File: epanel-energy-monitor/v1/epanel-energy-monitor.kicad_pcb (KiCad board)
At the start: 2 copper layers, 103 x 86.5 mm, 179 parts, among them J1 Conn_02x04_Odd_Even, J10 Screw_Terminal_01x02, J11 Screw_Terminal_01x02, J12 Screw_Terminal_01x02, J13 Screw_Terminal_01x02, J14 Screw_Terminal_01x02, J15 Screw_Terminal_01x02, J16 Screw_Terminal_01x02, J17 Screw_Terminal_01x02, J18 Screw_Terminal_01x02, J19 Screw_Terminal_01x02, J2 Screw_Terminal_01x02, J3 Conn_01x02_Male, J4 Screw_Terminal_01x02, J5 Screw_Terminal_01x02, J6 Screw_Terminal_01x02, J7 Screw_Terminal_01x02, J8 Screw_Terminal_01x02, J9 Screw_Terminal_01x02, Q1 BSS138, T1 230V - 6V, U1 LTV-814, U2 MCP3208, U3 MCP3208, U4 LMV321

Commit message: wip pcb
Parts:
- removed the R23 at (184.1, -34.2)
- removed the R24 at (184.3, -39.9)
- removed the R25 at (179.5, -39.8)
- removed the R26 at (184.3, -36.9)
- removed the R27 at (179.5, -36.9)
- removed the R28 at (179.5, -33.9)
- moved R11 100.3 mm to (134.7, 73.0)
- moved R12 100.3 mm to (134.9, 67.4)
- moved R13 100.3 mm to (130.5, 67.4)
- moved R14 100.3 mm to (134.9, 70.3)
- moved R15 100.3 mm to (130.5, 70.3)
- moved R16 100.3 mm to (130.5, 73.3)
- moved R29 98.5 mm to (166.3, 74.7)
- moved R30 98.5 mm to (166.5, 69.0)
- moved R31 98.5 mm to (162.1, 69.0)
- moved R32 98.5 mm to (166.5, 72.0)
- moved R33 98.5 mm to (162.1, 72.0)
- moved R34 98.5 mm to (162.1, 74.9)
- moved R35 94.4 mm to (177.1, 74.6)
- moved R36 94.4 mm to (177.3, 68.9)
- moved R37 94.4 mm to (172.9, 68.9)
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- renumbered R47 to R23, R48 to R24, R49 to R25, R50 to R26, R51 to R27, R52 to R28

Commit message: wip energy pcb
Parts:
- removed the R11 at (134.7, 73.0)
- removed the R12 at (134.9, 67.4)
- removed the R13 at (130.5, 67.4)
- removed the R14 at (134.9, 70.3)
- removed the R15 at (130.5, 70.3)
- removed the R16 at (130.5, 73.3)
- removed the R17 at (144.0, 71.8)
- removed the R18 at (144.2, 66.1)
- removed the R19 at (139.8, 66.1)
- removed the R20 at (144.2, 69.0)
- removed the R21 at (139.8, 69.0)
- removed the R22 at (139.8, 72.0)
- removed the R29 at (166.3, 74.7)
- removed the R30 at (166.5, 69.0)
- removed the R31 at (162.1, 69.0)
- removed the R32 at (166.5, 72.0)
- removed the R33 at (162.1, 72.0)
- removed the R34 at (162.1, 74.9)
- removed the R35 at (177.1, 74.6)
- removed the R36 at (177.3, 68.9)
- removed the R37 at (172.9, 68.9)
- removed the R38 at (177.3, 71.8)
- removed the R39 at (172.9, 71.8)
- removed the R40 at (172.9, 74.8)
- removed the R41 at (187.7, 72.7)
- removed the R42 at (187.9, 67.1)
- removed the R43 at (183.4, 67.1)
- removed the R44 at (187.9, 70.0)
- removed the R45 at (183.4, 70.0)
- removed the R46 at (183.4, 73.0)
- moved J3 21.8 mm to (130.2, 73.4), turned to 180 degrees
- moved T1 10.2 mm to (123.8, 68.5)
- renumbered R47 to R11, R48 to R12, R49 to R13, R50 to R14, R51 to R15, R52 to R16, R47 to R17, R48 to R18, R49 to R19, R50 to R20, R51 to R21, R52 to R22, R47 to R29, R48 to R30, R49 to R31, R50 to R32, R51 to R33, R52 to R34, R47 to R35, R48 to R36, R49 to R37, R50 to R38, R51 to R39, R52 to R40, R47 to R41, R48 to R42, R49 to R43, R50 to R44, R51 to R45, R52 to R46
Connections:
- R11 pad 1: /CT7 -> /CT1
- R11 pad 2: Net-(J11-Pad1) -> Net-(J5-Pad1)
- R12 pad 1: Net-(J11-Pad1) -> Net-(J5-Pad1)
- R12 pad 2: Net-(R48-Pad2) -> Net-(R12-Pad2)
- R13 pad 1: Net-(J11-Pad1) -> Net-(J5-Pad1)
- R13 pad 2: Net-(R49-Pad2) -> Net-(R13-Pad2)
- R14 pad 1: Net-(J11-Pad1) -> Net-(J5-Pad1)
- R14 pad 2: Net-(R50-Pad2) -> Net-(R14-Pad2)
- R15 pad 1: Net-(J11-Pad1) -> Net-(J5-Pad1)
- R15 pad 2: Net-(R51-Pad2) -> Net-(R15-Pad2)
- R16 pad 1: Net-(J11-Pad1) -> Net-(J5-Pad1)
- R16 pad 2: Net-(R52-Pad2) -> Net-(R16-Pad2)
- R17 pad 1: /CT7 -> /CT2
- R17 pad 2: Net-(J11-Pad1) -> Net-(J6-Pad1)
- R18 pad 1: Net-(J11-Pad1) -> Net-(J6-Pad1)
- R18 pad 2: Net-(R48-Pad2) -> Net-(R18-Pad2)
- R19 pad 1: Net-(J11-Pad1) -> Net-(J6-Pad1)
- R19 pad 2: Net-(R49-Pad2) -> Net-(R19-Pad2)
- R20 pad 1: Net-(J11-Pad1) -> Net-(J6-Pad1)
- R20 pad 2: Net-(R50-Pad2) -> Net-(R20-Pad2)
- R21 pad 1: Net-(J11-Pad1) -> Net-(J6-Pad1)
- R21 pad 2: Net-(R51-Pad2) -> Net-(R21-Pad2)
- R22 pad 1: Net-(J11-Pad1) -> Net-(J6-Pad1)
- R22 pad 2: Net-(R52-Pad2) -> Net-(R22-Pad2)
- R23 pad 1: /CT7 -> /CT3
- R23 pad 2: Net-(J11-Pad1) -> Net-(J7-Pad1)
- R24 pad 1: Net-(J11-Pad1) -> Net-(J7-Pad1)
- R24 pad 2: Net-(R48-Pad2) -> Net-(R24-Pad2)
- R25 pad 1: Net-(J11-Pad1) -> Net-(J7-Pad1)
- R25 pad 2: Net-(R49-Pad2) -> Net-(R25-Pad2)
- R26 pad 1: Net-(J11-Pad1) -> Net-(J7-Pad1)
- R26 pad 2: Net-(R50-Pad2) -> Net-(R26-Pad2)
- R27 pad 1: Net-(J11-Pad1) -> Net-(J7-Pad1)
- R27 pad 2: Net-(R51-Pad2) -> Net-(R27-Pad2)
- R28 pad 1: Net-(J11-Pad1) -> Net-(J7-Pad1)
- R28 pad 2: Net-(R52-Pad2) -> Net-(R28-Pad2)
- R29 pad 1: /CT7 -> /CT4
- R29 pad 2: Net-(J11-Pad1) -> Net-(J8-Pad1)
- R30 pad 1: Net-(J11-Pad1) -> Net-(J8-Pad1)
- R30 pad 2: Net-(R48-Pad2) -> Net-(R30-Pad2)
- R31 pad 1: Net-(J11-Pad1) -> Net-(J8-Pad1)
- R31 pad 2: Net-(R49-Pad2) -> Net-(R31-Pad2)
- R32 pad 1: Net-(J11-Pad1) -> Net-(J8-Pad1)
- R32 pad 2: Net-(R50-Pad2) -> Net-(R32-Pad2)
- R33 pad 1: Net-(J11-Pad1) -> Net-(J8-Pad1)
- R33 pad 2: Net-(R51-Pad2) -> Net-(R33-Pad2)
- R34 pad 1: Net-(J11-Pad1) -> Net-(J8-Pad1)
- R34 pad 2: Net-(R52-Pad2) -> Net-(R34-Pad2)
- R35 pad 1: /CT7 -> /CT5
- R35 pad 2: Net-(J11-Pad1) -> Net-(J9-Pad1)
- R36 pad 1: Net-(J11-Pad1) -> Net-(J9-Pad1)
- R36 pad 2: Net-(R48-Pad2) -> Net-(R36-Pad2)
- R37 pad 1: Net-(J11-Pad1) -> Net-(J9-Pad1)
- R37 pad 2: Net-(R49-Pad2) -> Net-(R37-Pad2)
- R38 pad 1: Net-(J11-Pad1) -> Net-(J9-Pad1)
- R38 pad 2: Net-(R50-Pad2) -> Net-(R38-Pad2)
- R39 pad 1: Net-(J11-Pad1) -> Net-(J9-Pad1)
- R39 pad 2: Net-(R51-Pad2) -> Net-(R39-Pad2)
- R40 pad 1: Net-(J11-Pad1) -> Net-(J9-Pad1)
- R40 pad 2: Net-(R52-Pad2) -> Net-(R40-Pad2)
- R41 pad 1: /CT7 -> /CT6
- R41 pad 2: Net-(J11-Pad1) -> Net-(J10-Pad1)
- R42 pad 1: Net-(J11-Pad1) -> Net-(J10-Pad1)
- R42 pad 2: Net-(R48-Pad2) -> Net-(R42-Pad2)
- R43 pad 1: Net-(J11-Pad1) -> Net-(J10-Pad1)
- R43 pad 2: Net-(R49-Pad2) -> Net-(R43-Pad2)
- R44 pad 1: Net-(J11-Pad1) -> Net-(J10-Pad1)
- R44 pad 2: Net-(R50-Pad2) -> Net-(R44-Pad2)
- R45 pad 1: Net-(J11-Pad1) -> Net-(J10-Pad1)
- R45 pad 2: Net-(R51-Pad2) -> Net-(R45-Pad2)
- R46 pad 1: Net-(J11-Pad1) -> Net-(J10-Pad1)
- R46 pad 2: Net-(R52-Pad2) -> Net-(R46-Pad2)
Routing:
- net Net-(J11-Pad1): track 233.0 -> 33.3 mm
- net Net-(R52-Pad2): track 102.0 -> 14.6 mm
- net Net-(R51-Pad2): track 91.2 -> 13.0 mm
- net Net-(R48-Pad2): track 89.8 -> 12.8 mm
- net Net-(R50-Pad2): track 85.0 -> 12.1 mm
- net Net-(R49-Pad2): track 81.1 -> 11.6 mm
- net Net-(J9-Pad1): track 0.00 -> 33.3 mm
- net Net-(J6-Pad1): track 0.00 -> 33.3 mm
- net Net-(J5-Pad1): track 0.00 -> 33.3 mm
- net Net-(J8-Pad1): track 0.00 -> 33.3 mm
- net Net-(J10-Pad1): track 0.00 -> 33.3 mm
- net Net-(J7-Pad1): track 0.00 -> 33.3 mm
- net Net-(R28-Pad2): track 0.00 -> 14.6 mm
- net Net-(R16-Pad2): track 0.00 -> 14.6 mm
- net Net-(R22-Pad2): track 0.00 -> 14.6 mm
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
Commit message: wip energy pcb
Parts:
- moved R1 171.8 mm to (108.9, 108.6), turned to 180 degrees
- moved D1 151.1 mm to (105.3, 108.6), turned to 180 degrees
- moved R3 137.7 mm to (110.5, 72.3)
- moved R4 113.5 mm to (108.8, 69.0)
- moved R7 112.3 mm to (108.1, 65.3)
- moved U1 110.6 mm to (109.7, 53.7)
- moved Q1 110.2 mm to (111.4, 61.3)
- moved R2 106.3 mm to (115.1, 65.4)
- moved D2 87.1 mm to (119.8, 43.0)
- moved C1 61.4 mm to (165.7, 12.7)
- moved R5 61.4 mm to (172.0, 8.26)
- moved R8 61.4 mm to (165.7, 15.2)
- moved R9 61.4 mm to (150.1, 15.7)
- moved U2 61.4 mm to (173.9, 1.28)
- moved U3 61.4 mm to (165.4, 1.28)
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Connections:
- J18 pad 2: /CT Sensor 9/ZERO -> /CT Sensor 1/ZERO
- R89 pad 1: /CT Sensor 9/SENSE -> /CT9
- S14 pad 2: /CT Sensor 9/ZERO -> /CT Sensor 1/ZERO
- S14 pad 7: /CT Sensor 9/ZERO -> /CT Sensor 1/ZERO
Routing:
- net /CT Sensor 1/ZERO: track 242.9 -> 311.6 mm
- net /TIC: track 0.00 -> 34.1 mm
- net /CT Sensor 9/ZERO: track 17.4 -> 0.00 mm
- net +3V3: track 0.00 -> 9.87 mm
- net GND: track 0.00 -> 8.65 mm
- net Net-(D1-Pad1): track 0.00 -> 1.90 mm

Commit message: wip pcb
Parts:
- moved R9 101.1 mm to (224.3, 84.4)
- moved C1 88.4 mm to (223.8, 79.4)
- moved R10 88.4 mm to (238.2, 66.0)
- moved R5 88.4 mm to (230.0, 74.9)
- moved R6 88.4 mm to (238.2, 68.5)
- moved R8 88.4 mm to (223.8, 81.9)
- moved U2 88.4 mm to (232.0, 67.9)
- moved U3 88.4 mm to (223.5, 67.9)
- moved U4 88.4 mm to (220.6, 75.9)
- moved T1 34.5 mm to (111.8, 67.9), turned to 0 degrees
- moved R3 23.6 mm to (113.7, 48.9), turned to 180 degrees
- moved R4 17.3 mm to (120.0, 55.9), turned to 180 degrees
- moved R2 16.7 mm to (117.5, 48.9)
- moved R7 16.5 mm to (109.9, 48.9), turned to 180 degrees
- moved Q1 12.2 mm to (120.0, 52.7), turned to 90 degrees
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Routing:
- net Net-(J4-Pad2): track 0.00 -> 46.9 mm
- net Net-(J2-Pad2): track 0.00 -> 31.3 mm
- net Net-(J4-Pad1): track 0.00 -> 29.8 mm
- net Net-(J2-Pad1): track 0.00 -> 17.0 mm
- net +3V3: track 9.87 -> 22.9 mm
- net /TIC: track 34.1 -> 41.4 mm
- net Net-(Q1-Pad1): track 0.00 -> 6.99 mm
- net Net-(D2-Pad1): track 0.00 -> 6.87 mm
- net Net-(R7-Pad2): track 0.00 -> 5.53 mm
- net /CT Sensor 1/ZERO: track 311.6 -> 316.0 mm
- net GND: track 8.65 -> 10.9 mm

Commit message: wip pcb
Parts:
- moved R10 96.1 mm to (142.4, 73.7)
- moved R6 95.8 mm to (142.4, 69.8)
- moved R5 88.0 mm to (142.4, 67.9), turned to 180 degrees
- moved U4 85.0 mm to (135.9, 68.6)
- moved R9 82.4 mm to (142.4, 75.6), turned to 180 degrees
- moved C1 81.8 mm to (142.4, 71.8), turned to 180 degrees
- moved R8 81.6 mm to (142.4, 77.5), turned to 180 degrees
- moved J3 17.1 mm to (136.0, 76.8)
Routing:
- net /CT Sensor 1/ZERO: track 316.0 -> 411.9 mm
- net +3V3: track 22.9 -> 116.3 mm, vias 0 -> 4
- net GND: track 10.9 -> 91.5 mm
- net /TIC: track 41.4 -> 93.1 mm, vias 0 -> 2
- net Net-(J3-Pad1): track 0.00 -> 15.7 mm
- net Net-(C1-Pad1): track 0.00 -> 13.2 mm
- net Net-(R10-Pad2): track 0.00 -> 4.75 mm

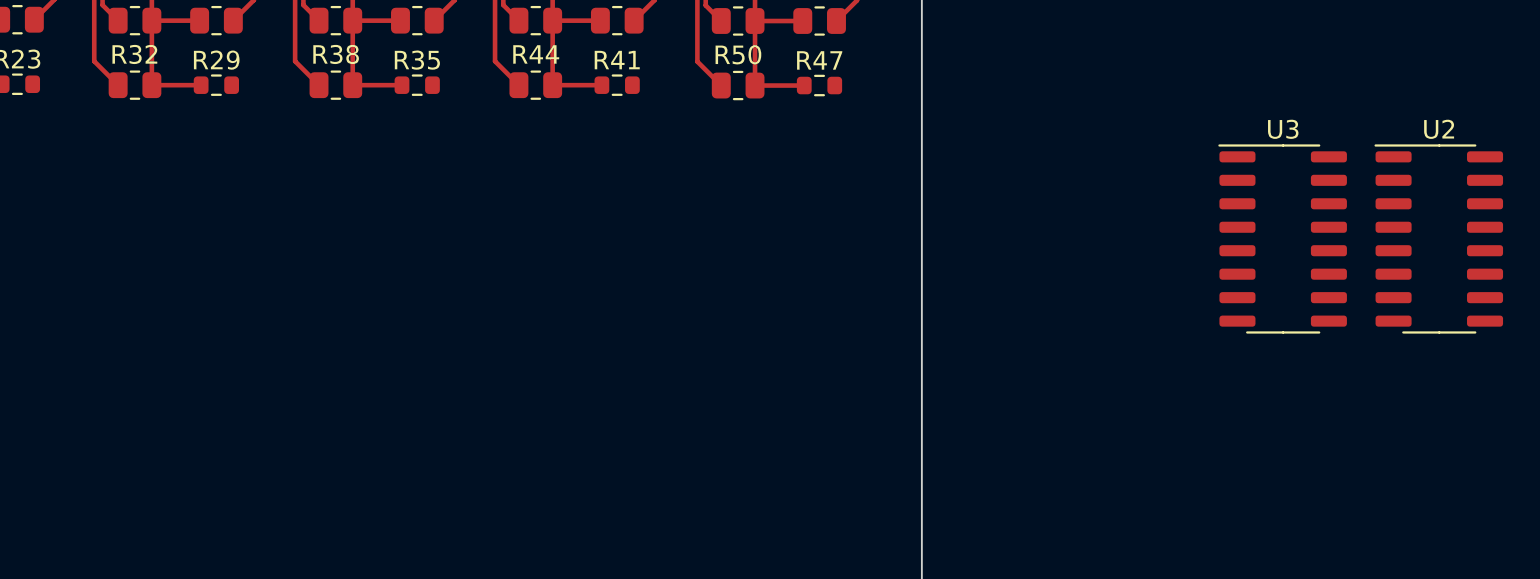
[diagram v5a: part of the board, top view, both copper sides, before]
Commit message: fix annotations
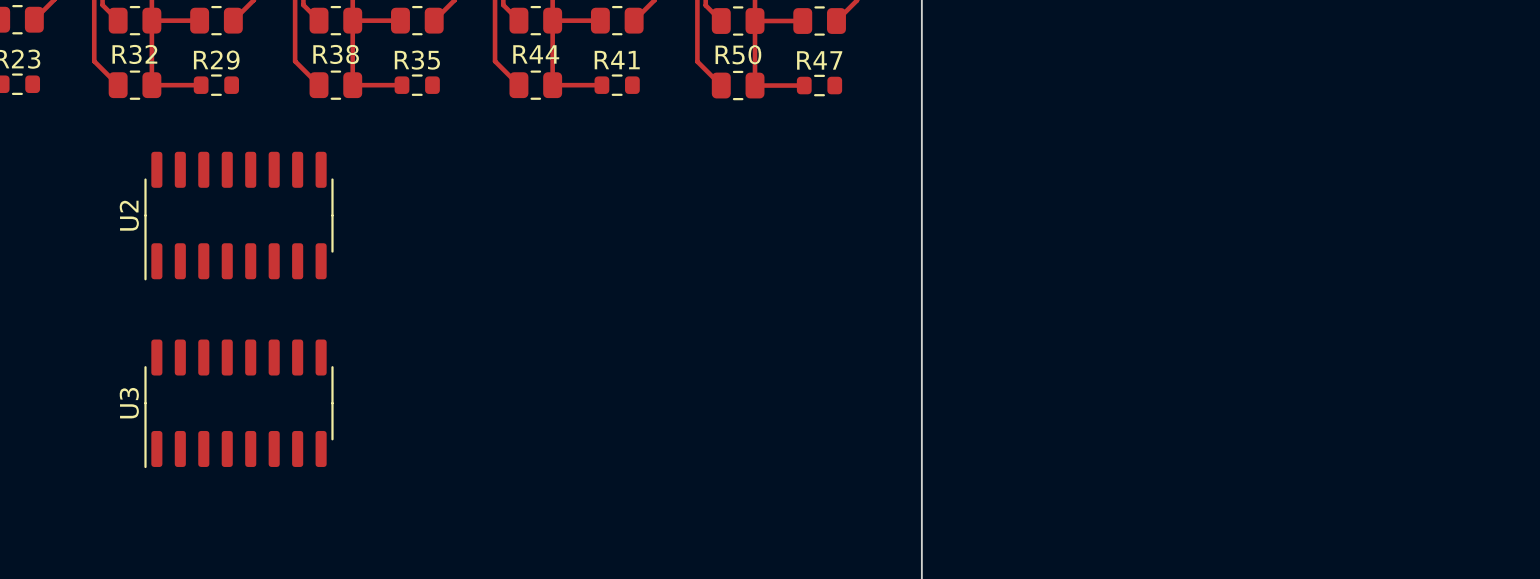
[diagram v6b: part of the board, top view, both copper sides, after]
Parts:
- moved U2 65.0 mm to (167.0, 66.7), turned to 90 degrees
- moved U3 57.2 mm to (167.0, 76.8), turned to 90 degrees
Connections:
- R59 pad 1: /CT14 -> /CT9
- R77 pad 1: /CT13 -> /CT12
- R83 pad 1: /CT12 -> /CT13
- R89 pad 1: /CT9 -> /CT14

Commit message: wip pcb
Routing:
- net GND: track 91.5 -> 160.8 mm, vias 0 -> 4
- net /CT8: track 0.00 -> 45.5 mm
- net +3V3: track 116.3 -> 157.5 mm, vias 4 -> 5
- net /CT9: track 0.00 -> 36.6 mm
- net /CT1: track 0.00 -> 33.9 mm
- net /CT15: track 0.00 -> 33.8 mm
- net /CT7: track 0.00 -> 31.7 mm
- net /CT14: track 0.00 -> 28.1 mm
- net /CT10: track 0.00 -> 27.4 mm
- net /CT2: track 0.00 -> 24.3 mm
- net Net-(R8-Pad1): track 0.00 -> 22.8 mm
- net /CT6: track 0.00 -> 22.3 mm
- net /CT4: track 0.00 -> 19.8 mm
- net /CT11: track 0.00 -> 19.1 mm
- net /CT13: track 0.00 -> 18.2 mm
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
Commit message: wip pcb
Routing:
- net /SCLK: track 14.1 -> 97.9 mm
- net /MISO: track 14.1 -> 97.4 mm
- net /MOSI: track 14.1 -> 96.8 mm
- net GND: track 160.8 -> 159.0 mm
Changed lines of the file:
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@@
   (via (at 165.1 62.23) (size 0.8) (drill 0.4) (layers "F.Cu" "B.Cu") (net 1))
   (segment (start 121.03 68.58) (end 120.84 68.39) (width 0.25) (layer "B.Cu") (net 1))
-  (segment (start 165.1 62.23) (end 163.83 60.96) (width 0.25) (layer "B.Cu") (net 1))
   (segment (start 144.145 68.58) (end 132.715 68.58) (width 0.25) (layer "B.Cu") (net 1))
   (segment (start 163.83 73.66) (end 149.225 73.66) (width 0.25) (layer "B.Cu") (net 1))
@@
   (via (at 166.37 72.39) (size 0.8) (drill 0.4) (layers "F.Cu" "B.Cu") (net 5))
   (segment (start 166.37 62.23) (end 166.37 72.39) (width 0.25) (layer "B.Cu") (net 5))
+  (segment (start 166.37 72.39) (end 155.575 83.185) (width 0.25) (layer "B.Cu") (net 5))
+  (segment (start 155.575 83.185) (end 125.095 83.185) (width 0.25) (layer "B.Cu") (net 5))
+  (segment (start 125.095 83.185) (end 107.6198 100.6602) (width 0.25) (layer "B.Cu") (net 5))
+  (segment (start 107.6198 100.6602) (end 107.6198 113.9952) (width 0.25) (layer "B.Cu") (net 5))
   (segment (start 167.64 64.2) (end 167.64 62.23) (width 0.25) (layer "F.Cu") (net 7))
   (segment (start 167.64 74.36) (end 167.64 72.39) (width 0.25) (layer "F.Cu") (net 7))
@@
   (via (at 167.64 72.39) (size 0.8) (drill 0.4) (layers "F.Cu" "B.Cu") (net 7))
   (segment (start 167.64 62.23) (end 167.64 72.39) (width 0.25) (layer "B.Cu") (net 7))
+  (segment (start 125.73 83.82) (end 110.1598 99.3902) (width 0.25) (layer "B.Cu") (net 7))
+  (segment (start 167.64 72.39) (end 156.21 83.82) (width 0.25) (layer "B.Cu") (net 7))
+  (segment (start 156.21 83.82) (end 125.73 83.82) (width 0.25) (layer "B.Cu") (net 7))
+  (segment (start 110.1598 99.3902) (end 110.1598 113.9952) (width 0.25) (layer "B.Cu") (net 7))
   (segment (start 127.87 76.835) (end 126.76 77.945) (width 0.25) (layer "F.Cu") (net 9))
   (segment (start 140.2375 76.835) (end 135.9875 76.835) (width 0.25) (layer "F.Cu") (net 9))
@@
   (via (at 168.91 62.23) (size 0.8) (drill 0.4) (layers "F.Cu" "B.Cu") (net 10))
   (via (at 168.91 72.39) (size 0.8) (drill 0.4) (layers "F.Cu" "B.Cu") (net 10))
+  (segment (start 126.365 84.455) (end 112.6998 98.1202) (width 0.25) (layer "B.Cu") (net 10))
+  (segment (start 168.91 72.39) (end 156.845 84.455) (width 0.25) (layer "B.Cu") (net 10))
   (segment (start 168.91 62.23) (end 168.91 72.39) (width 0.25) (layer "B.Cu") (net 10))
+  (segment (start 156.845 84.455) (end 126.365 84.455) (width 0.25) (layer "B.Cu") (net 10))
+  (segment (start 112.6998 98.1202) (end 112.6998 113.9952) (width 0.25) (layer "B.Cu") (net 10))
   (segment (start 143.192 71.755) (end 143.192 69.85) (width 0.25) (layer "F.Cu") (net 11))
   (segment (start 134.7525 67.63) (end 135.7075 66.675) (width 0.25) (layer "F.Cu") (net 11))
